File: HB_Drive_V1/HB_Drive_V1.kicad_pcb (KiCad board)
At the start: 2 copper layers, 15 parts, among them J1 Conn_02x05_Counter_Clockwise, U1 TL082, U2 TL082

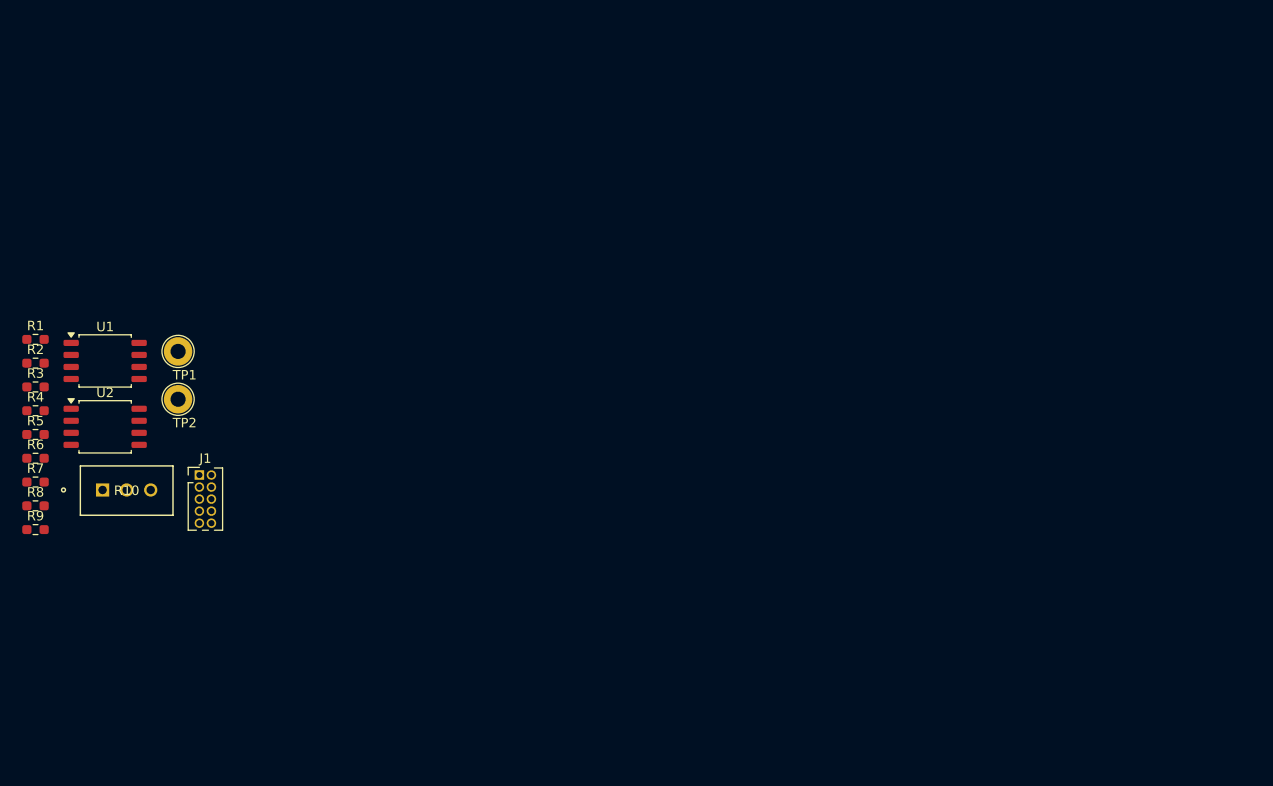
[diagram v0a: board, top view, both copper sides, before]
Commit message: adds 10v reference and DC offsets / gain control to I_fdbk and V_fdbk
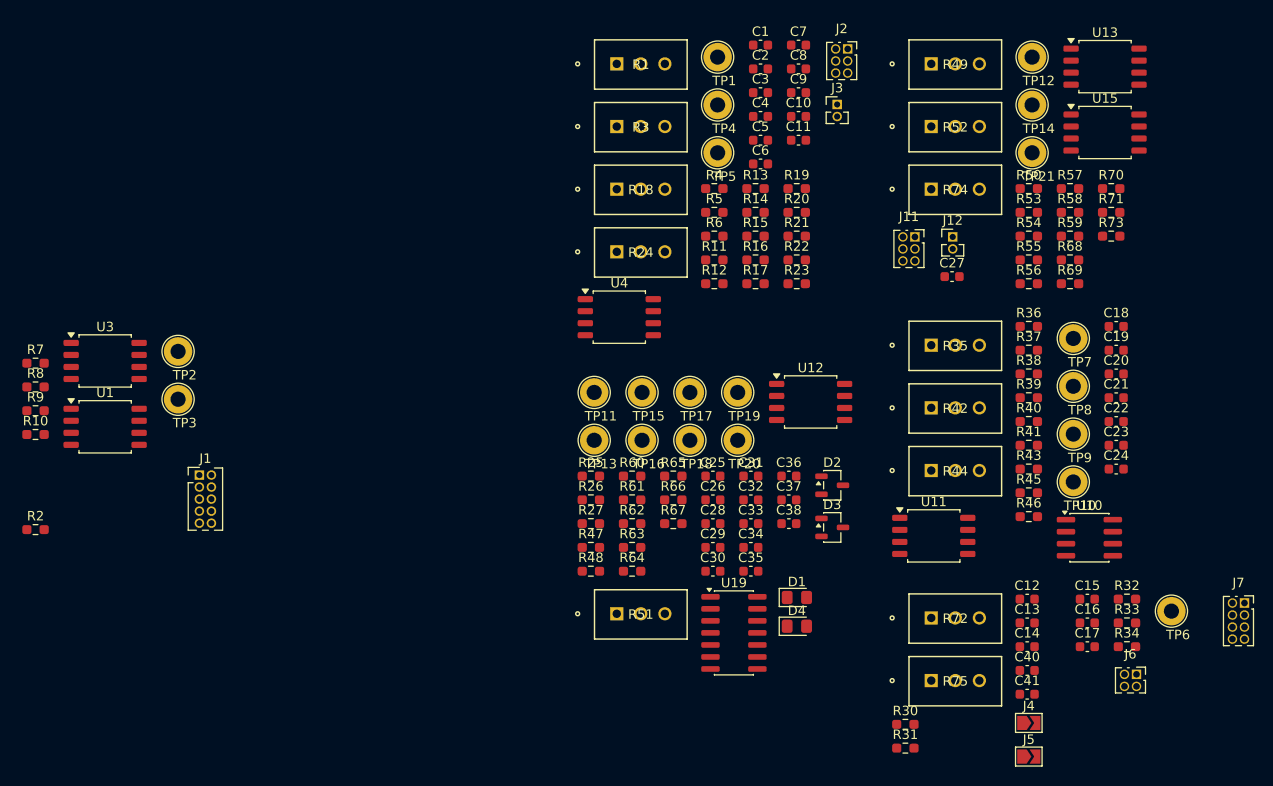
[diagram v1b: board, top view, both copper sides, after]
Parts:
- removed the R10 at (120.3, 97.2)
- removed the R7 at (113.2, 96.4)
- removed the R8 at (113.2, 98.9)
- added C1: 27uF 5%, Capacitor_SMD:C_0603_1608Metric, F.Cu at (189.7, 50.3)
- added C10: 100nF 100V, Capacitor_SMD:C_0603_1608Metric, F.Cu at (193.7, 57.8)
- added C11: 100nF 100V, Capacitor_SMD:C_0603_1608Metric, F.Cu at (193.7, 60.3)
- added C12: 470pF 50V, Capacitor_SMD:C_0603_1608Metric, F.Cu at (217.9, 108.8)
- added C13: 470pF 50V, Capacitor_SMD:C_0603_1608Metric, F.Cu at (217.9, 111.3)
- added C14: 100nF 100V, Capacitor_SMD:C_0603_1608Metric, F.Cu at (217.9, 113.8)
- added C15: 100nF 100V, Capacitor_SMD:C_0603_1608Metric, F.Cu at (224.2, 108.8)
- added C16: 100nF 100V, Capacitor_SMD:C_0603_1608Metric, F.Cu at (224.2, 111.3)
- added C17: 100nF 100V, Capacitor_SMD:C_0603_1608Metric, F.Cu at (224.2, 113.8)
- added C18: 100pF 50V, Capacitor_SMD:C_0603_1608Metric, F.Cu at (227.3, 80.0)
- added C19: 100nF 100V, Capacitor_SMD:C_0603_1608Metric, F.Cu at (227.3, 82.5)
- added C2: 27uF 5%, Capacitor_SMD:C_0603_1608Metric, F.Cu at (189.7, 52.8)
- added C20: 100nF 100V, Capacitor_SMD:C_0603_1608Metric, F.Cu at (227.3, 85.0)
- added C21: 100pF 50V, Capacitor_SMD:C_0603_1608Metric, F.Cu at (227.3, 87.5)
- added C22: 100pF 50V, Capacitor_SMD:C_0603_1608Metric, F.Cu at (227.3, 90.0)
- added C23: 100nF 100V, Capacitor_SMD:C_0603_1608Metric, F.Cu at (227.3, 92.5)
- added C24: 100nF 100V, Capacitor_SMD:C_0603_1608Metric, F.Cu at (227.3, 95.0)
- added C25: 100nF 100V, Capacitor_SMD:C_0603_1608Metric, F.Cu at (184.7, 95.8)
- added C26: 100nF 100V, Capacitor_SMD:C_0603_1608Metric, F.Cu at (184.7, 98.3)
- added C27: 10uF 5%, Capacitor_SMD:C_0603_1608Metric, F.Cu at (209.9, 74.7)
- added C28: 100nF 100V, Capacitor_SMD:C_0603_1608Metric, F.Cu at (184.7, 100.8)
- added C29: 100nF 100V, Capacitor_SMD:C_0603_1608Metric, F.Cu at (184.7, 103.3)
- added C3: 10uF 5%, Capacitor_SMD:C_0603_1608Metric, F.Cu at (189.7, 55.3)
- added C30: 100nF 100V, Capacitor_SMD:C_0603_1608Metric, F.Cu at (184.7, 105.8)
- added C31: 100nF 100V, Capacitor_SMD:C_0603_1608Metric, F.Cu at (188.7, 95.8)
- added C32: 100pF, Capacitor_SMD:C_0603_1608Metric, F.Cu at (188.7, 98.3)
- added C33: 100nF 100V, Capacitor_SMD:C_0603_1608Metric, F.Cu at (188.7, 100.8)
- added C34: 100nF 100V, Capacitor_SMD:C_0603_1608Metric, F.Cu at (188.7, 103.3)
- added C35: 100nF 100V, Capacitor_SMD:C_0603_1608Metric, F.Cu at (188.7, 105.8)
- added C36: 100nF 100V, Capacitor_SMD:C_0603_1608Metric, F.Cu at (192.7, 95.8)
- added C37: 100nF 100V, Capacitor_SMD:C_0603_1608Metric, F.Cu at (192.7, 98.3)
- added C38: 100nF 100V, Capacitor_SMD:C_0603_1608Metric, F.Cu at (192.7, 100.8)
- added C4: 100nF 100V, Capacitor_SMD:C_0603_1608Metric, F.Cu at (189.7, 57.8)
- added C40: 100nF 100V, Capacitor_SMD:C_0603_1608Metric, F.Cu at (217.9, 116.3)
- added C41: 100nF 100V, Capacitor_SMD:C_0603_1608Metric, F.Cu at (217.9, 118.8)
- added C5: 100nF 100V, Capacitor_SMD:C_0603_1608Metric, F.Cu at (189.7, 60.3)
- added C6: 100nF 100V, Capacitor_SMD:C_0603_1608Metric, F.Cu at (189.7, 62.8)
- added C7: 100nF 100V, Capacitor_SMD:C_0603_1608Metric, F.Cu at (193.7, 50.3)
- added C8: 100nF 100V, Capacitor_SMD:C_0603_1608Metric, F.Cu at (193.7, 52.8)
- added C9: 100nF 100V, Capacitor_SMD:C_0603_1608Metric, F.Cu at (193.7, 55.3)
- added D1: RED [XL-2012SURC], LED_SMD:LED_0805_2012Metric_Pad1.15x1.40mm_HandSolder, F.Cu at (193.6, 108.6)
- added D2: MMBD914LT3G, Package_TO_SOT_SMD:SOT-23-3, F.Cu at (197.3, 96.7)
- added D3: MMBD914LT3G, Package_TO_SOT_SMD:SOT-23-3, F.Cu at (197.3, 101.2)
- added D4: GREEN [XL-2012UGC], LED_SMD:LED_0805_2012Metric_Pad1.15x1.40mm_HandSolder, F.Cu at (193.6, 111.6)
- added J11: Conn_02x03_Counter_Clockwise, Connector_PinSocket_1.27mm:PinSocket_2x03_P1.27mm_Vertical, F.Cu at (206.0, 70.5)
- added J12: Conn_01x02, Connector_PinHeader_1.27mm:PinHeader_1x02_P1.27mm_Vertical, F.Cu at (210.0, 70.5)
- added J2: Conn_02x03_Counter_Clockwise, Connector_PinSocket_1.27mm:PinSocket_2x03_P1.27mm_Vertical, F.Cu at (198.9, 50.7)
- added J3: Conn_01x02, Connector_PinHeader_1.27mm:PinHeader_1x02_P1.27mm_Vertical, F.Cu at (197.8, 56.5)
- added J4: Conn_01x02, Jumper:SolderJumper-2_P1.3mm_Open_TrianglePad1.0x1.5mm, F.Cu at (218.0, 121.8)
- added J5: Conn_01x02, Jumper:SolderJumper-2_P1.3mm_Open_TrianglePad1.0x1.5mm, F.Cu at (218.0, 125.4)
- added J6: Conn_02x02_Odd_Even, Connector_PinSocket_1.27mm:PinSocket_2x02_P1.27mm_Vertical, F.Cu at (229.4, 116.7)
- added J7: Conn_02x04_Counter_Clockwise, Connector_PinSocket_1.27mm:PinSocket_2x04_P1.27mm_Vertical, F.Cu at (240.8, 109.2)
- added R11: 976kΩ 1%, Resistor_SMD:R_0603_1608Metric_Pad0.98x0.95mm_HandSolder, F.Cu at (184.8, 73.0)
- added R12: 1MΩ 5%, Resistor_SMD:R_0603_1608Metric_Pad0.98x0.95mm_HandSolder, F.Cu at (184.8, 75.5)
- added R13: 10kΩ, Resistor_SMD:R_0603_1608Metric_Pad0.98x0.95mm_HandSolder, F.Cu at (189.2, 65.4)
- added R14: 402kΩ 1%, Resistor_SMD:R_0603_1608Metric_Pad0.98x0.95mm_HandSolder, F.Cu at (189.2, 67.9)
- added R15: 6.65kΩ 1%, Resistor_SMD:R_0603_1608Metric_Pad0.98x0.95mm_HandSolder, F.Cu at (189.2, 70.4)
- added R16: 10kΩ, Resistor_SMD:R_0603_1608Metric_Pad0.98x0.95mm_HandSolder, F.Cu at (189.2, 73.0)
- added R17: 10kΩ 1%, Resistor_SMD:R_0603_1608Metric_Pad0.98x0.95mm_HandSolder, F.Cu at (189.2, 75.5)
- added R18: PV36W104C01B00, PV36W104C01B00:POT_PV36W_BRN, F.Cu at (174.5, 65.5)
- added R19: 10kΩ, Resistor_SMD:R_0603_1608Metric_Pad0.98x0.95mm_HandSolder, F.Cu at (193.5, 65.4)
- added R20: 10kΩ, Resistor_SMD:R_0603_1608Metric_Pad0.98x0.95mm_HandSolder, F.Cu at (193.5, 67.9)
- added R21: 10K, Resistor_SMD:R_0603_1608Metric_Pad0.98x0.95mm_HandSolder, F.Cu at (193.5, 70.4)
- added R22: 10K, Resistor_SMD:R_0603_1608Metric_Pad0.98x0.95mm_HandSolder, F.Cu at (193.5, 73.0)
- added R23: 10kΩ, Resistor_SMD:R_0603_1608Metric_Pad0.98x0.95mm_HandSolder, F.Cu at (193.5, 75.5)
- added R24: PV36W104C01B00, PV36W104C01B00:POT_PV36W_BRN, F.Cu at (174.5, 72.1)
- added R25: 10KΩ, Resistor_SMD:R_0603_1608Metric_Pad0.98x0.95mm_HandSolder, F.Cu at (171.8, 95.8)
- added R26: 10KΩ, Resistor_SMD:R_0603_1608Metric_Pad0.98x0.95mm_HandSolder, F.Cu at (171.8, 98.3)
- added R27: 10KΩ, Resistor_SMD:R_0603_1608Metric_Pad0.98x0.95mm_HandSolder, F.Cu at (171.8, 100.8)
- added R3: PV36W104C01B00, PV36W104C01B00:POT_PV36W_BRN, F.Cu at (174.5, 58.9)
- added R30: 100KΩ, Resistor_SMD:R_0603_1608Metric_Pad0.98x0.95mm_HandSolder, F.Cu at (205.0, 122.0)
- added R31: 100KΩ, Resistor_SMD:R_0603_1608Metric_Pad0.98x0.95mm_HandSolder, F.Cu at (205.0, 124.5)
- added R32: 1KΩ, Resistor_SMD:R_0603_1608Metric_Pad0.98x0.95mm_HandSolder, F.Cu at (228.4, 108.8)
- added R33: 1KΩ, Resistor_SMD:R_0603_1608Metric_Pad0.98x0.95mm_HandSolder, F.Cu at (228.4, 111.3)
- added R34: 1KΩ, Resistor_SMD:R_0603_1608Metric_Pad0.98x0.95mm_HandSolder, F.Cu at (228.4, 113.8)
- added R35: PV36W104C01B00, PV36W104C01B00:POT_PV36W_BRN, F.Cu at (207.7, 82.0)
- added R36: 1KΩ, Resistor_SMD:R_0603_1608Metric_Pad0.98x0.95mm_HandSolder, F.Cu at (218.0, 80.0)
- added R37: 51KΩ, Resistor_SMD:R_0603_1608Metric_Pad0.98x0.95mm_HandSolder, F.Cu at (218.0, 82.5)
- added R38: 51KΩ, Resistor_SMD:R_0603_1608Metric_Pad0.98x0.95mm_HandSolder, F.Cu at (218.0, 85.0)
- added R39: 51KΩ, Resistor_SMD:R_0603_1608Metric_Pad0.98x0.95mm_HandSolder, F.Cu at (218.0, 87.5)
- added R4: 301kΩ 1%, Resistor_SMD:R_0603_1608Metric_Pad0.98x0.95mm_HandSolder, F.Cu at (184.8, 65.4)
- added R40: 10KΩ, Resistor_SMD:R_0603_1608Metric_Pad0.98x0.95mm_HandSolder, F.Cu at (218.0, 90.0)
- added R41: 51KΩ, Resistor_SMD:R_0603_1608Metric_Pad0.98x0.95mm_HandSolder, F.Cu at (218.0, 92.5)
- added R42: PV36W104C01B00, PV36W104C01B00:POT_PV36W_BRN, F.Cu at (207.7, 88.6)
- added R43: 100KΩ, Resistor_SMD:R_0603_1608Metric_Pad0.98x0.95mm_HandSolder, F.Cu at (218.0, 95.0)
- added R44: PV36W104C01B00, PV36W104C01B00:POT_PV36W_BRN, F.Cu at (207.7, 95.2)
- added R45: 10KΩ, Resistor_SMD:R_0603_1608Metric_Pad0.98x0.95mm_HandSolder, F.Cu at (218.0, 97.5)
- added R46: 1MΩ 5%, Resistor_SMD:R_0603_1608Metric_Pad0.98x0.95mm_HandSolder, F.Cu at (218.0, 100.1)
- added R47: 10KΩ, Resistor_SMD:R_0603_1608Metric_Pad0.98x0.95mm_HandSolder, F.Cu at (171.8, 103.3)
- added R48: 10KΩ, Resistor_SMD:R_0603_1608Metric_Pad0.98x0.95mm_HandSolder, F.Cu at (171.8, 105.8)
- added R49: PV36W104C01B00, PV36W104C01B00:POT_PV36W_BRN, F.Cu at (207.7, 52.3)
- added R5: 10.2kΩ 1%, Resistor_SMD:R_0603_1608Metric_Pad0.98x0.95mm_HandSolder, F.Cu at (184.8, 67.9)
- added R50: 10K, Resistor_SMD:R_0603_1608Metric_Pad0.98x0.95mm_HandSolder, F.Cu at (218.0, 65.4)
- added R51: PV36W104C01B00, PV36W104C01B00:POT_PV36W_BRN, F.Cu at (174.5, 110.3)
- added R52: PV36W104C01B00, PV36W104C01B00:POT_PV36W_BRN, F.Cu at (207.7, 58.9)
- added R53: 10kΩ, Resistor_SMD:R_0603_1608Metric_Pad0.98x0.95mm_HandSolder, F.Cu at (218.0, 67.9)
- added R54: 10K, Resistor_SMD:R_0603_1608Metric_Pad0.98x0.95mm_HandSolder, F.Cu at (218.0, 70.4)
- added R55: 10K, Resistor_SMD:R_0603_1608Metric_Pad0.98x0.95mm_HandSolder, F.Cu at (218.0, 73.0)
- added R56: 10K, Resistor_SMD:R_0603_1608Metric_Pad0.98x0.95mm_HandSolder, F.Cu at (218.0, 75.5)
- added R57: 10K, Resistor_SMD:R_0603_1608Metric_Pad0.98x0.95mm_HandSolder, F.Cu at (222.4, 65.4)
- added R58: 1MΩ 5%, Resistor_SMD:R_0603_1608Metric_Pad0.98x0.95mm_HandSolder, F.Cu at (222.4, 67.9)
- added R59: 10kΩ, Resistor_SMD:R_0603_1608Metric_Pad0.98x0.95mm_HandSolder, F.Cu at (222.4, 70.4)
- added R60: 10KΩ, Resistor_SMD:R_0603_1608Metric_Pad0.98x0.95mm_HandSolder, F.Cu at (176.2, 95.8)
- added R61: 10KΩ, Resistor_SMD:R_0603_1608Metric_Pad0.98x0.95mm_HandSolder, F.Cu at (176.2, 98.3)
- added R62: 1KΩ, Resistor_SMD:R_0603_1608Metric_Pad0.98x0.95mm_HandSolder, F.Cu at (176.2, 100.8)
- added R63: 100Ω, Resistor_SMD:R_0603_1608Metric_Pad0.98x0.95mm_HandSolder, F.Cu at (176.2, 103.3)
- added R64: 1KΩ, Resistor_SMD:R_0603_1608Metric_Pad0.98x0.95mm_HandSolder, F.Cu at (176.2, 105.8)
- added R65: 470Ω, Resistor_SMD:R_0603_1608Metric_Pad0.98x0.95mm_HandSolder, F.Cu at (180.5, 95.8)
- added R66: 470Ω, Resistor_SMD:R_0603_1608Metric_Pad0.98x0.95mm_HandSolder, F.Cu at (180.5, 98.3)
- added R67: 1KΩ, Resistor_SMD:R_0603_1608Metric_Pad0.98x0.95mm_HandSolder, F.Cu at (180.5, 100.8)
- added R68: 10kΩ, Resistor_SMD:R_0603_1608Metric_Pad0.98x0.95mm_HandSolder, F.Cu at (222.4, 73.0)
- added R69: 10kΩ, Resistor_SMD:R_0603_1608Metric_Pad0.98x0.95mm_HandSolder, F.Cu at (222.4, 75.5)
- added R70: 10kΩ, Resistor_SMD:R_0603_1608Metric_Pad0.98x0.95mm_HandSolder, F.Cu at (226.7, 65.4)
- added R71: 10K, Resistor_SMD:R_0603_1608Metric_Pad0.98x0.95mm_HandSolder, F.Cu at (226.7, 67.9)
- added R72: PV36W502C01B00, PV36W104C01B00:POT_PV36W_BRN, F.Cu at (207.7, 110.8)
- added R73: 10kΩ, Resistor_SMD:R_0603_1608Metric_Pad0.98x0.95mm_HandSolder, F.Cu at (226.7, 70.4)
- added R74: PV36W104C01B00, PV36W104C01B00:POT_PV36W_BRN, F.Cu at (207.7, 65.5)
- added R75: PV36W502C01B00, PV36W104C01B00:POT_PV36W_BRN, F.Cu at (207.7, 117.4)
- added TP1: TestPoint, TestPoint:TestPoint_Loop_D2.60mm_Drill1.6mm_Beaded, F.Cu at (185.2, 51.5)
- added TP10: TestPoint, TestPoint:TestPoint_Loop_D2.60mm_Drill1.6mm_Beaded, F.Cu at (222.7, 96.4)
- added TP11: TestPoint, TestPoint:TestPoint_Loop_D2.60mm_Drill1.6mm_Beaded, F.Cu at (172.2, 86.9)
- added TP12: TestPoint, TestPoint:TestPoint_Loop_D2.60mm_Drill1.6mm_Beaded, F.Cu at (218.4, 51.5)
- added TP13: TestPoint, TestPoint:TestPoint_Loop_D2.60mm_Drill1.6mm_Beaded, F.Cu at (172.2, 92.0)
- added TP14: TestPoint, TestPoint:TestPoint_Loop_D2.60mm_Drill1.6mm_Beaded, F.Cu at (218.4, 56.6)
- added TP15: TestPoint, TestPoint:TestPoint_Loop_D2.60mm_Drill1.6mm_Beaded, F.Cu at (177.2, 86.9)
- added TP16: TestPoint, TestPoint:TestPoint_Loop_D2.60mm_Drill1.6mm_Beaded, F.Cu at (177.2, 92.0)
- added TP17: TestPoint, TestPoint:TestPoint_Loop_D2.60mm_Drill1.6mm_Beaded, F.Cu at (182.3, 86.9)
- added TP18: TestPoint, TestPoint:TestPoint_Loop_D2.60mm_Drill1.6mm_Beaded, F.Cu at (182.3, 92.0)
- added TP19: TestPoint, TestPoint:TestPoint_Loop_D2.60mm_Drill1.6mm_Beaded, F.Cu at (187.3, 86.9)
- added TP20: TestPoint, TestPoint:TestPoint_Loop_D2.60mm_Drill1.6mm_Beaded, F.Cu at (187.3, 92.0)
- added TP21: TestPoint, TestPoint:TestPoint_Loop_D2.60mm_Drill1.6mm_Beaded, F.Cu at (218.4, 61.6)
- added TP4: TestPoint, TestPoint:TestPoint_Loop_D2.60mm_Drill1.6mm_Beaded, F.Cu at (185.2, 56.6)
- added TP5: TestPoint, TestPoint:TestPoint_Loop_D2.60mm_Drill1.6mm_Beaded, F.Cu at (185.2, 61.6)
- added TP6: TestPoint, TestPoint:TestPoint_Loop_D2.60mm_Drill1.6mm_Beaded, F.Cu at (233.1, 110.0)
- added TP7: TestPoint, TestPoint:TestPoint_Loop_D2.60mm_Drill1.6mm_Beaded, F.Cu at (222.7, 81.2)
- added TP8: TestPoint, TestPoint:TestPoint_Loop_D2.60mm_Drill1.6mm_Beaded, F.Cu at (222.7, 86.3)
- added TP9: TestPoint, TestPoint:TestPoint_Loop_D2.60mm_Drill1.6mm_Beaded, F.Cu at (222.7, 91.3)
- added U10: NE555D, Package_SO:SOIC-8_3.9x4.9mm_P1.27mm, F.Cu at (224.4, 102.3)
- added U11: TL082, Package_SO:SOIC-8_5.3x5.3mm_P1.27mm, F.Cu at (208.0, 102.1)
- added U12: TL082, Package_SO:SOIC-8_5.3x5.3mm_P1.27mm, F.Cu at (195.0, 88.0)
- added U13: TL082, Package_SO:SOIC-8_5.3x5.3mm_P1.27mm, F.Cu at (226.1, 52.5)
- added U15: TL082, Package_SO:SOIC-8_5.3x5.3mm_P1.27mm, F.Cu at (226.1, 59.5)
- added U19: 74LS32, Package_SO:SOIC-14_3.9x8.7mm_P1.27mm, F.Cu at (186.9, 112.3)
- added U4: TL082, Package_SO:SOIC-8_5.3x5.3mm_P1.27mm, F.Cu at (174.8, 79.0)
- R1: value 10K -> PV36W104C01B00; footprint Resistor_SMD:R_0603_1608Metric_Pad0.98x0.95mm_HandSolder -> PV36W104C01B00:POT_PV36W_BRN
- R6: value 10K -> 10kΩ
- moved R6 75.4 mm to (184.8, 70.4)
- moved R1 67.9 mm to (174.5, 52.3)
- renumbered R5 to R10, R9 to R2, R2 to R7, R3 to R8, R4 to R9, TP1 to TP2, TP2 to TP3, U2 to U1, U1 to U3
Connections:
- R1 pad 1: Net-(J1-Pin_10) -> /Inner Current Regulator/+I_Err
- R1 pad 2: Net-(U1A--) (its old number) -> Net-(U1B--)
- R10 pad 2: Net-(U1A--) (its old number) -> Net-(U3A--)
- R6 pad 1: Net-(U1A--) (its old number) -> Net-(U3A--)
- R6 pad 2: Net-(R6-Pad2) -> Net-(J1-Pin_10)
- R7 pad 2: Net-(U1A--) (its old number) -> Net-(U3A--)
- R8 pad 2: Net-(U1A--) (its old number) -> Net-(U3A--)
- R9 pad 2: Net-(U1A--) (its old number) -> Net-(U3A--)
- TP2 pad 1: Net-(R6-Pad2) -> Net-(R13-Pad1)
- U1 pad 1: unconnected-(U2-Pad1) -> /Inner Current Regulator/Prop_Reg_Cmd
- U1 pad 4: (no net) -> -15V
- U1 pad 5: (no net) -> GND
- U1 pad 6: (no net) -> Net-(U1B--)
- U1 pad 7: (no net) -> /Inner Current Regulator/Int_Reg_Cmd
- U1 pad 8: (no net) -> +15V
- U3 pad 1: Net-(R6-Pad2) -> Net-(R13-Pad1)
- U3 pad 2: Net-(U1A--) (its old number) -> Net-(U3A--)
- U3 pad 4: unconnected-(U1C-V--Pad4) -> -15V
- U3 pad 8: unconnected-(U1C-V+-Pad8) -> +15V
